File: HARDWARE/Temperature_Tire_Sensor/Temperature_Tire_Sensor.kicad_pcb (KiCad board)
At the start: 4 copper layers, 42 parts, among them IC1 MLX90621ESF-BAB-000-SP, J1 SWD_01x06, J2 CAN_01x04, SW1 RESET, U1 STM32L4P5RET6, U2 MIC5236, U3 MIC5306-2.6YD5-TR, U4 SN65HVD232, Y1 16MGHz

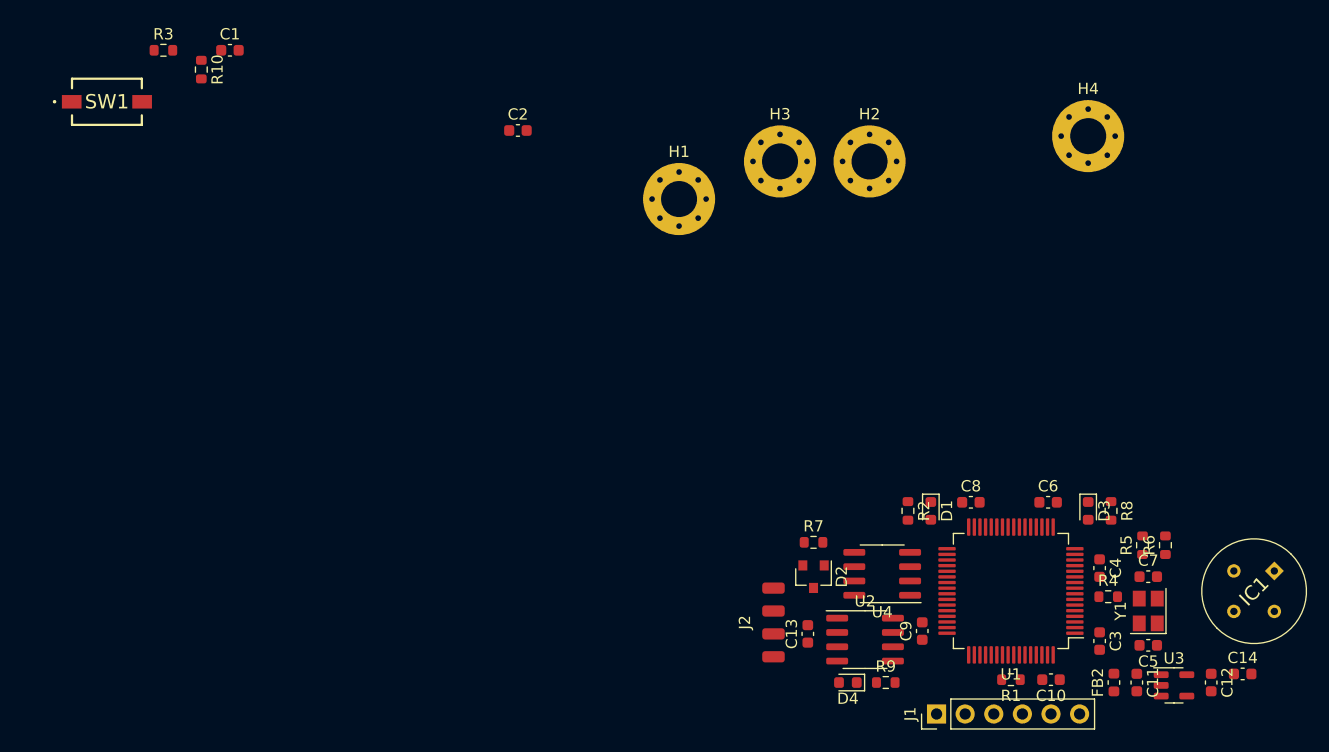
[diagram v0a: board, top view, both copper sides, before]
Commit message: pcb layout is done/has to be checked
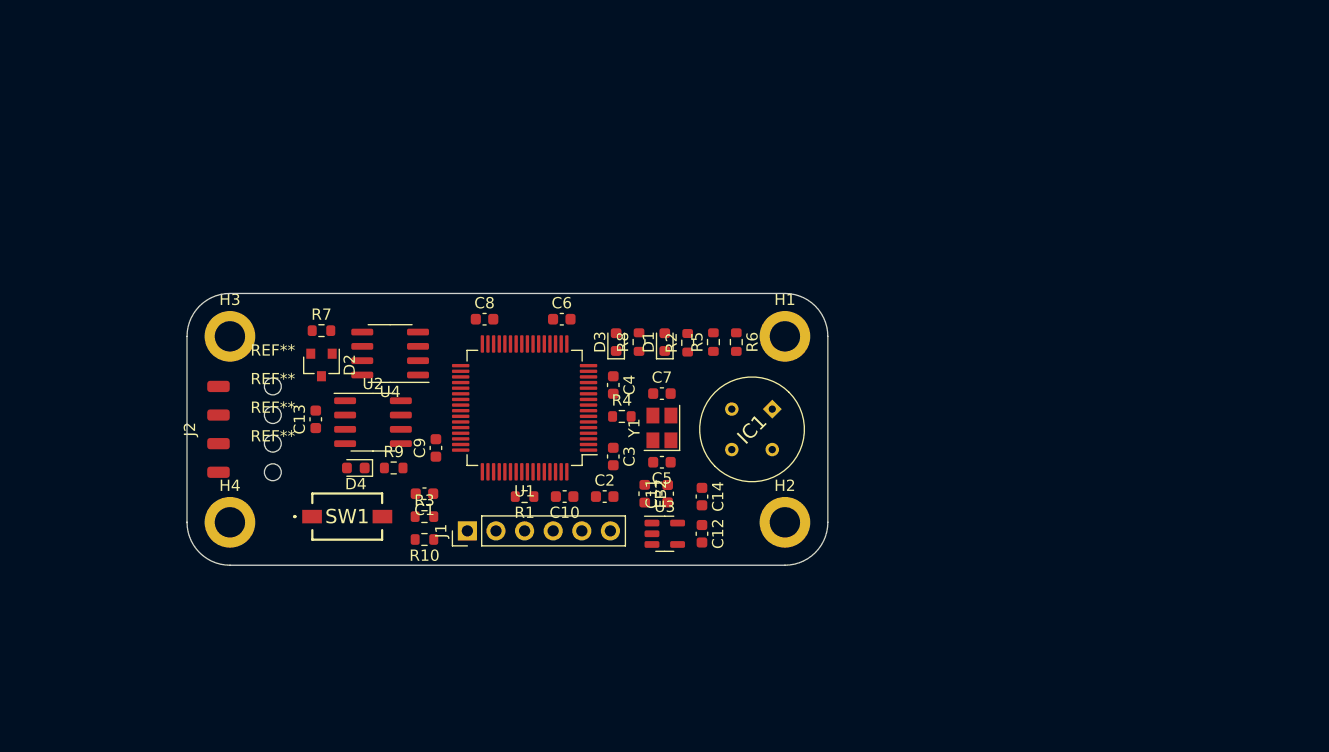
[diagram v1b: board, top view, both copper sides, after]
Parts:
- added REF**: MountingHole_2.1mm, MountingHole:MountingHole_2.1mm, F.Cu at (120.7, 111.1)
- added REF**: MountingHole_2.1mm, MountingHole:MountingHole_2.1mm, F.Cu at (120.7, 108.6)
- added REF**: MountingHole_2.1mm, MountingHole:MountingHole_2.1mm, F.Cu at (120.7, 116.2)
- added REF**: MountingHole_2.1mm, MountingHole:MountingHole_2.1mm, F.Cu at (120.7, 113.7)
- H1, H2, H3, H4: footprint MountingHole:MountingHole_3.2mm_M3_Pad_Via -> MountingHole:MountingHole_2.7mm_M2.5_ISO14580_Pad
- moved H4 83.6 mm to (116.8, 120.7)
- moved J2 52.2 mm to (115.8, 112.4)
- moved H3 51.2 mm to (116.8, 104.1)
- moved C14 50.5 mm to (158.8, 118.4), turned to -90 degrees
- moved U4 47.9 mm to (131.1, 105.7)
- moved U2 47.8 mm to (129.5, 111.8)
- moved D4 47.7 mm to (128.0, 115.8)
- moved C13 47.7 mm to (124.5, 111.5)
- moved R9 47.7 mm to (131.4, 115.8)
- moved D2 47.6 mm to (125.0, 106.7)
- moved R7 47.6 mm to (125.0, 103.6)
- moved R3 47.4 mm to (134.1, 120.1)
- moved U3 47.2 mm to (155.4, 121.7)
- moved C12 47.1 mm to (158.8, 121.7)
- moved IC1 46.8 mm to (165.0, 110.6)
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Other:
- board outline added: 56.9 x 24.1 mm

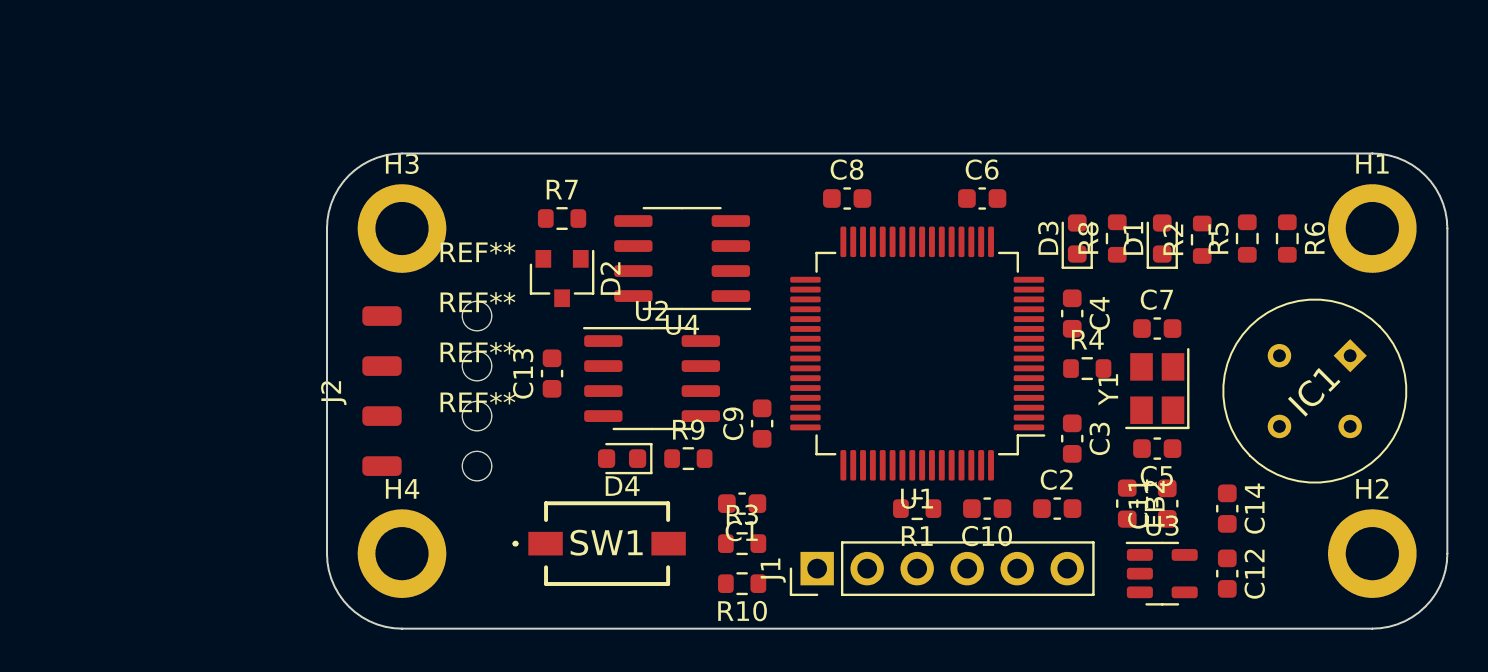
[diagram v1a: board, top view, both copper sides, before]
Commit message: Routing is done - has to be checked
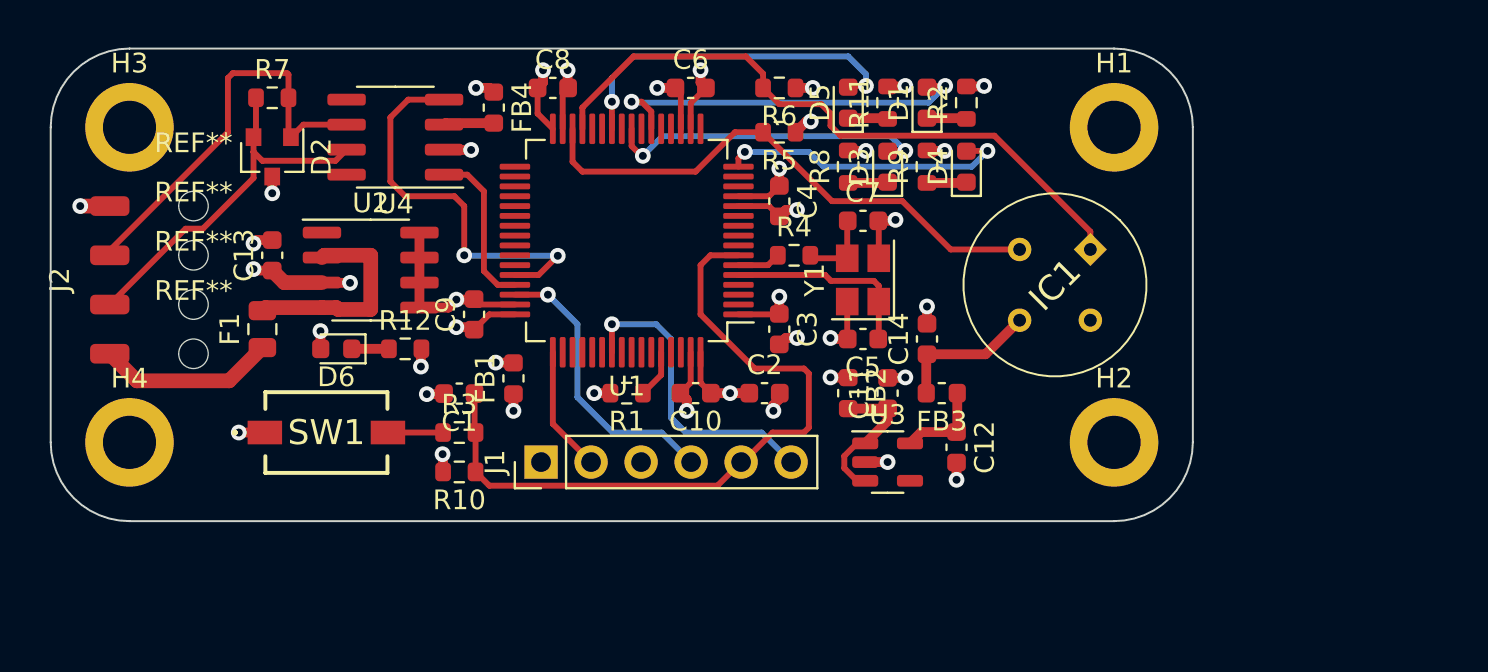
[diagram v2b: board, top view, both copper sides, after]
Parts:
- added D5: GREEN, Diode_SMD:D_0603_1608Metric, F.Cu at (139.5, 97.8)
- added D6: RED, Diode_SMD:D_0603_1608Metric, F.Cu at (113.5, 110.2)
- added F1: Polyfuse, Fuse:Fuse_0805_2012Metric, F.Cu at (109.8, 109.2)
- added FB1: 60R@100MHz, Inductor_SMD:L_0603_1608Metric, F.Cu at (122.5, 111.8)
- added FB3: 60R@100MHz, Inductor_SMD:L_0603_1608Metric, F.Cu at (144.2, 112.5)
- added FB4: 60R@100MHz, Inductor_SMD:L_0603_1608Metric, F.Cu at (121.5, 98.0)
- added R11: 1k5, Resistor_SMD:R_0603_1608Metric, F.Cu at (141.5, 97.8)
- added R12: 1k5, Resistor_SMD:R_0603_1608Metric, F.Cu at (117.0, 110.2)
- D1: value BLUE -> RED
- D3, D4: value RED -> YELLOW
- moved R6 26.9 mm to (136.0, 97.0), turned to 180 degrees
- moved R5 24.4 mm to (136.0, 99.2), turned to 180 degrees
- moved D4 22.9 mm to (145.5, 101.0), turned to 90 degrees
- moved R9 19.1 mm to (143.5, 101.0), turned to 90 degrees
- moved C14 17.5 mm to (143.5, 109.8), turned to 90 degrees
- moved C2 16.0 mm to (135.2, 112.5)
- moved C8 16.0 mm to (124.5, 97.0)
- moved D2 16.0 mm to (110.2, 100.5)
- moved R4 16.0 mm to (136.8, 105.5)
- moved C5 15.9 mm to (140.2, 109.8)
- moved R7 15.9 mm to (110.2, 97.5)
- moved C4 15.9 mm to (136.0, 102.8)
- moved Y1 15.9 mm to (140.2, 106.8)
- moved C10 15.9 mm to (131.8, 112.5)
- moved C7 15.9 mm to (140.2, 103.8)
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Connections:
- C10 pad 1: +3V3 -> /+3V3_uC
- C14 pad 1: +2V6 -> Net-(C14-Pad1)
- C2 pad 1: +3V3 -> /+3V3_uC
- C3 pad 1: +3V3 -> /+3V3_uC
- C4 pad 1: +3V3 -> /+3V3_uC
- C6 pad 1: +3V3 -> /+3V3_uC
- C8 pad 1: +3V3 -> /+3V3_uC
- C9 pad 1: +3V3 -> /+3V3_uC
- D1 pad 2: /LED -> /LED_ERR
- D3 pad 2: /LED_ERR -> /LED_WAR1
- D4 pad 2: +3V3 -> /LED_WAR2
- IC1 pad 3: +2V6 -> Net-(C14-Pad1)
- U1 pad 1: +3V3 -> /+3V3_uC
- U1 pad 13: +3V3 -> /+3V3_uC
- U1 pad 16: unconnected-(U1-Pad16) -> /LED_WAR2
- U1 pad 19: +3V3 -> /+3V3_uC
- U1 pad 24: unconnected-(U1-Pad24) -> /LED_WAR1
- U1 pad 26: /LED -> /LED_OK
- U1 pad 32: +3V3 -> /+3V3_uC
- U1 pad 48: +3V3 -> /+3V3_uC
- U1 pad 64: +3V3 -> /+3V3_uC
- U2 pad 2: +24V -> Net-(F1-Pad2)
- U2 pad 4: +24V -> Net-(F1-Pad2)
- U4 pad 3: +3V3 -> Net-(FB4-Pad2)
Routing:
- net GND: track 0.00 -> 45.9 mm, vias 0 -> 25
- net /NRST: track 0.00 -> 36.6 mm
- net /SCL: track 0.00 -> 33.4 mm
- net /SDA: track 0.00 -> 27.9 mm
- net /+3V3_uC: track 0.00 -> 21.5 mm, vias 0 -> 7
- net /CAN_L: track 0.00 -> 21.0 mm
- net /CAN_RX: track 0.00 -> 20.2 mm, vias 0 -> 2
- net /LED_ERR: track 0.00 -> 19.5 mm, vias 0 -> 2
- net /CAN_H: track 0.00 -> 19.2 mm
- net /LED_OK: track 0.00 -> 17.8 mm, vias 0 -> 2
- net /LED_WAR1: track 0.00 -> 16.6 mm, vias 0 -> 2
- net /SWO: track 0.00 -> 15.8 mm, vias 0 -> 1
- net /LED_WAR2: track 0.00 -> 14.9 mm, vias 0 -> 2
- net /SWDIO: track 0.00 -> 14.6 mm, vias 0 -> 1
- net +3V3: track 0.00 -> 11.6 mm, vias 0 -> 9
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- added copper zone on In2.Cu, net +3V3
- added copper zone on In2.Cu, net /+3V3_uC
- added copper zone on In1.Cu, net GND
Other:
- board size 56.9 x 24.1 mm -> 58 x 24 mm
